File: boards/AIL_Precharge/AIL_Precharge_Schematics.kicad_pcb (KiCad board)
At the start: 2 copper layers, 17 parts, among them J1 Ultrafit_2, J2 Ultrafit_2, J3 Ultrafit_2, J4 Ultrafit_2, J5 Ultrafit_2, K1 G2RL-1-E, Q1 SSM3K333R, U1 NCP785AH150T1G

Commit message: add finalized pcb, schematics, gerber and drill files for AIL_Precharge
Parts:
- moved R3 2.94 mm to (139.4, 107.1)
- moved D1 0.09 mm to (120.9, 98.4), turned to 270 degrees
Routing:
- net Net-(D1-Pad1): track 60.9 -> 23.4 mm, vias 0 -> 2
- net Net-(D2-Pad2): track 16.7 -> 7.82 mm, vias 0 -> 2
- net Net-(F1-Pad2): track 41.2 -> 45.9 mm
- net Net-(F2-Pad1): track 30.1 -> 34.4 mm
- net Net-(D2-Pad1): track 19.0 -> 15.3 mm, vias 0 -> 2
- net Net-(Q1-Pad1): track 14.7 -> 18.3 mm
- net Net-(J2-Pad2): track 9.84 -> 8.79 mm
- net Net-(D1-Pad2): track 21.1 -> 20.2 mm
- net Net-(J2-Pad1): track 18.5 -> 17.7 mm
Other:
- board outline added: 67.1 x 50 mm
- board text added: "OEM AIL PRECHARGE SHERRIE SHEN"
- board text removed: "OEM AIL PRECHARGE"

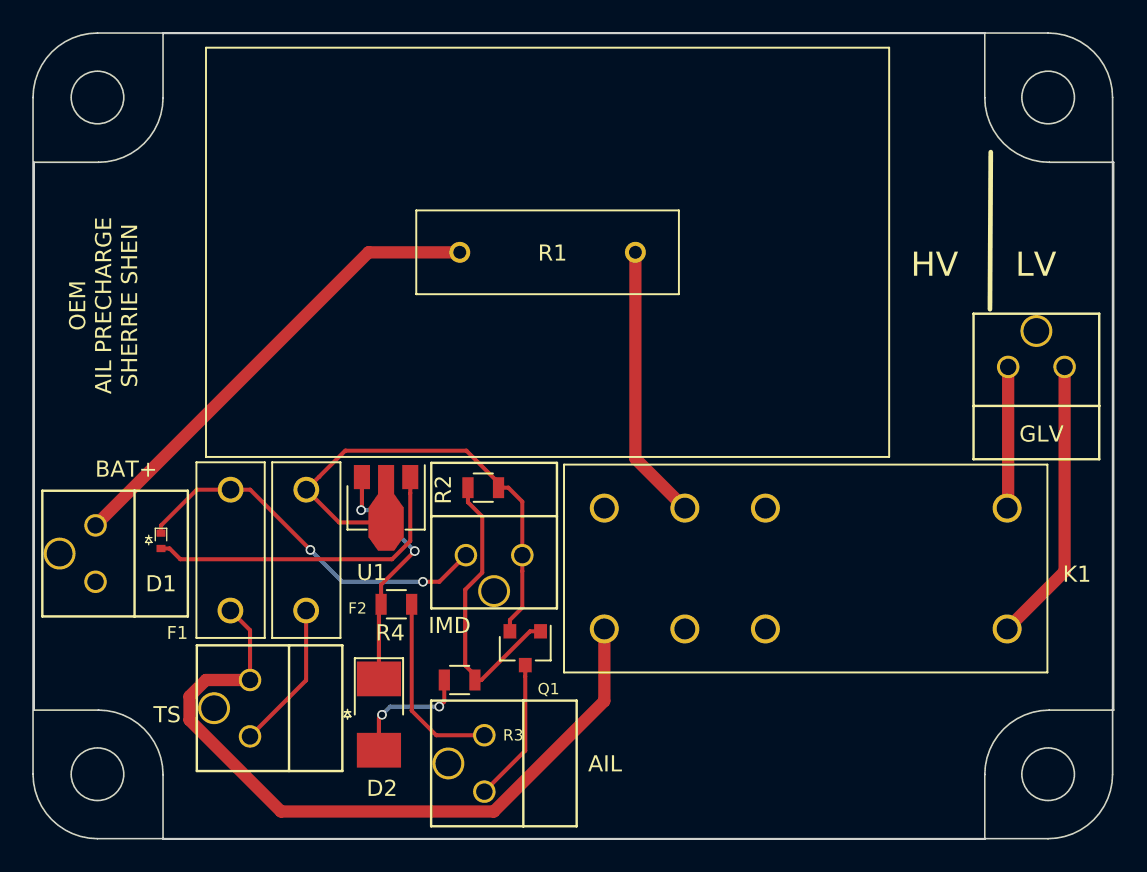
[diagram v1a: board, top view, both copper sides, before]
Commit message: add 3d models
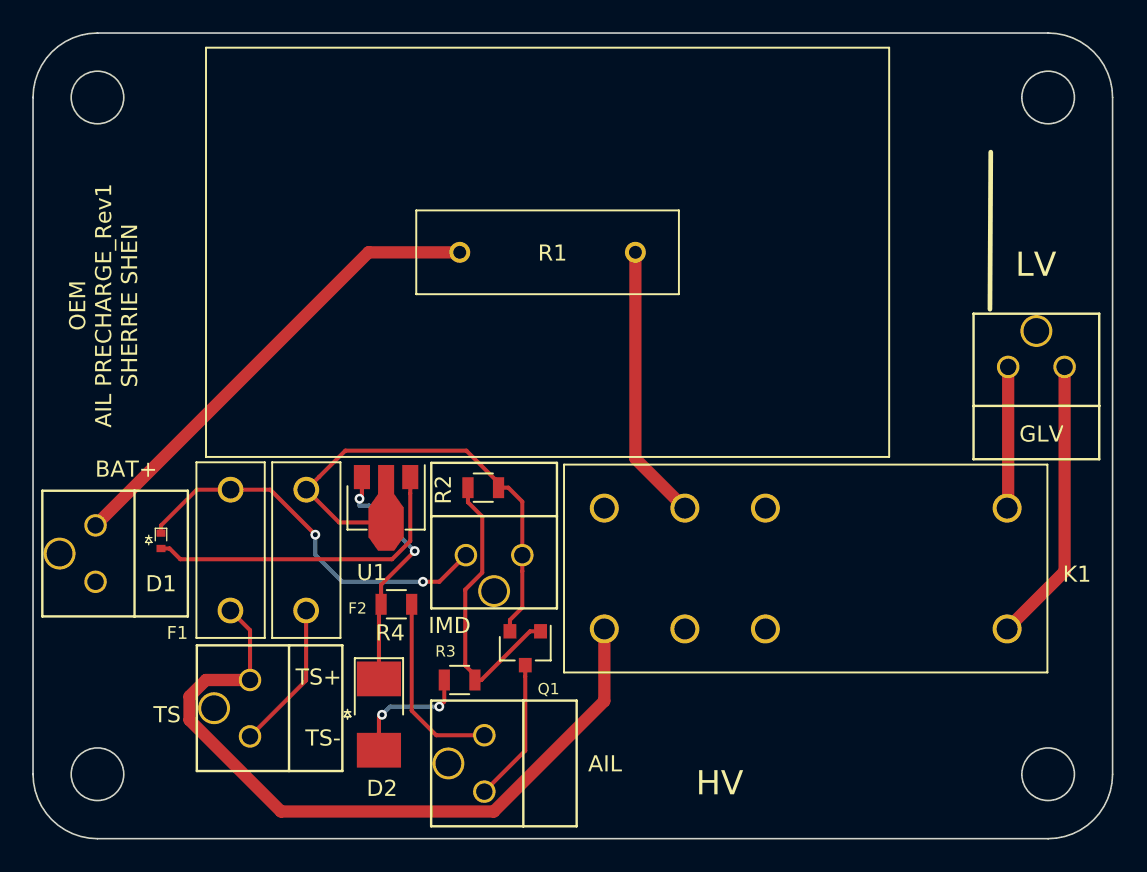
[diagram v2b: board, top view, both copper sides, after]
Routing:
- net Net-(D1-Pad1): track 23.4 -> 24.1 mm
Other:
- board size 67.1 x 50 mm -> 67 x 50 mm
- net class Default: via_dia 0.6 -> 0.6096; via_drill 0.4 -> 0.3048
- rule via_min_drill: 0.3 -> 0.3048
- rule via_min_size: 0.4 -> 0.6096
- board text added: "OEM AIL PRECHARGE_Rev1 SHERRIE SHEN"
- board text added: "TS+"
- board text added: "TS-"
- board text removed: "OEM AIL PRECHARGE SHERRIE SHEN"
